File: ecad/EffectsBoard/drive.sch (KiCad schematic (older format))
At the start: 11 parts, among them U1 RC4558

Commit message: Rearrange schematics
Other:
- moved on the sheet: 51p1, C5, C6, D2, D3, R10, R7, R8, R9, RV1, U1A

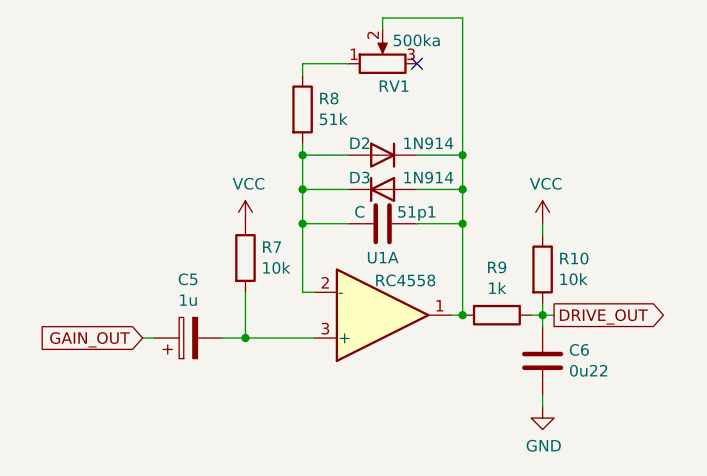
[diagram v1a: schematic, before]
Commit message: Fix annotation
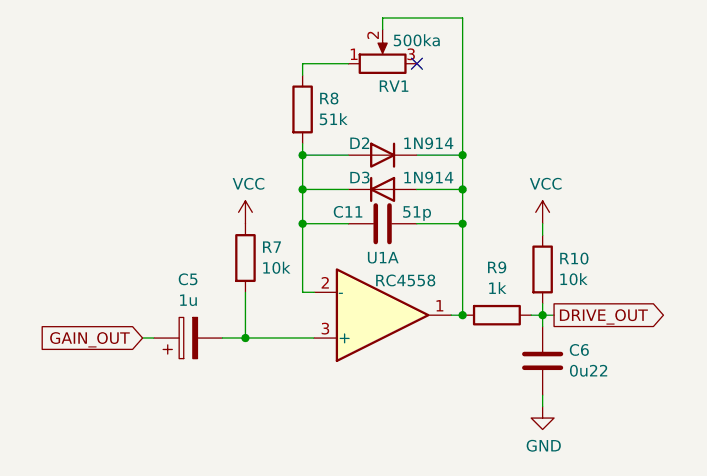
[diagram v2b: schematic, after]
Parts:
- C11: renamed from 51p1; value C -> 51p
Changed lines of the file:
@@
 P 1950 1400
 AR Path="/60325725" Ref="51p?"  Part="1"
-AR Path="/603069E8/60325725" Ref="51p1"  Part="1"
-F 0 "51p1" V 1900 1550 50  0000 C CNN
-F 1 "C" V 1900 1300 50  0000 C CNN
+AR Path="/603069E8/60325725" Ref="C11"  Part="1"
+F 0 "C11" V 1900 1250 50  0000 C CNN
+F 1 "51p" V 1900 1550 50  0000 C CNN
 F 2 "" H 1988 1250 50  0001 C CNN
 F 3 "~" H 1950 1400 50  0001 C CNN

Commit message: Update ecad autosave
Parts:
- C11, C5, C6: footprint (none) -> Capacitor_SMD:C_0805_2012Metric_Pad1.18x1.45mm_HandSolder
- R10, R7, R8, R9: footprint (none) -> Resistor_SMD:R_0805_2012Metric_Pad1.20x1.40mm_HandSolder
- RV1: footprint (none) -> screaming-panda:Potentiometer_Bourns_PTV09A-1_Single_Vertical
- U1: footprint (none) -> Package_SO:Texas_R-PDSO-G8_EP2.95x4.9mm_Mask2.4x3.1mm
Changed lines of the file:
@@
 F 0 "C5" V 1355 1900 50  0000 C CNN
 F 1 "1u" V 1264 1900 50  0000 C CNN
-F 2 "" H 1138 1750 50  0001 C CNN
+F 2 "Capacitor_SMD:C_0805_2012Metric_Pad1.18x1.45mm_HandSolder" H 1138 1750 50  0001 C CNN
 F 3 "~" H 1100 1900 50  0001 C CNN
 	1    1100 1900
@@
 F 0 "U1" H 1950 1550 50  0000 C CNN
 F 1 "RC4558" H 2050 1650 50  0000 C CNN
-F 2 "" H 1950 1800 50  0001 C CNN
+F 2 "Package_SO:Texas_R-PDSO-G8_EP2.95x4.9mm_Mask2.4x3.1mm" H 1950 1800 50  0001 C CNN
 F 3 "http://www.ti.com/lit/ds/symlink/rc4558.pdf" H 1950 1800 50  0001 C CNN
 	1    1950 1800
@@
 F 0 "C11" V 1900 1250 50  0000 C CNN
 F 1 "51p" V 1900 1550 50  0000 C CNN
-F 2 "" H 1988 1250 50  0001 C CNN
+F 2 "Capacitor_SMD:C_0805_2012Metric_Pad1.18x1.45mm_HandSolder" H 1988 1250 50  0001 C CNN
 F 3 "~" H 1950 1400 50  0001 C CNN
 	1    1950 1400
@@
 F 0 "R8" H 1670 946 50  0000 L CNN
 F 1 "51k" H 1670 855 50  0000 L CNN
-F 2 "" V 1530 900 50  0001 C CNN
+F 2 "Resistor_SMD:R_0805_2012Metric_Pad1.20x1.40mm_HandSolder" V 1530 900 50  0001 C CNN
 F 3 "~" H 1600 900 50  0001 C CNN
 	1    1600 900
@@
 F 0 "RV1" V 1850 650 50  0000 C CNN
 F 1 "500ka" V 2050 550 50  0000 C CNN
-F 2 "" H 1950 700 50  0001 C CNN
+F 2 "screaming-panda:Potentiometer_Bourns_PTV09A-1_Single_Vertical" H 1950 700 50  0001 C CNN
 F 3 "~" H 1950 700 50  0001 C CNN
 	1    1950 700
@@
 F 0 "R9" V 2243 1800 50  0000 C CNN
 F 1 "1k" V 2334 1800 50  0000 C CNN
-F 2 "" V 2380 1800 50  0001 C CNN
+F 2 "Resistor_SMD:R_0805_2012Metric_Pad1.20x1.40mm_HandSolder" V 2380 1800 50  0001 C CNN
 F 3 "~" H 2450 1800 50  0001 C CNN
 	1    2450 1800
@@
 F 0 "R10" H 2720 1646 50  0000 L CNN
 F 1 "10k" H 2720 1555 50  0000 L CNN
-F 2 "" V 2580 1600 50  0001 C CNN
+F 2 "Resistor_SMD:R_0805_2012Metric_Pad1.20x1.40mm_HandSolder" V 2580 1600 50  0001 C CNN
 F 3 "~" H 2650 1600 50  0001 C CNN
 	1    2650 1600
@@
 F 0 "C6" H 2765 2046 50  0000 L CNN
 F 1 "0u22" H 2765 1955 50  0000 L CNN
-F 2 "" H 2688 1850 50  0001 C CNN
+F 2 "Capacitor_SMD:C_0805_2012Metric_Pad1.18x1.45mm_HandSolder" H 2688 1850 50  0001 C CNN
 F 3 "~" H 2650 2000 50  0001 C CNN
 	1    2650 2000
@@
 F 0 "R7" H 1420 1596 50  0000 L CNN
 F 1 "10k" H 1420 1505 50  0000 L CNN
-F 2 "" V 1280 1550 50  0001 C CNN
+F 2 "Resistor_SMD:R_0805_2012Metric_Pad1.20x1.40mm_HandSolder" V 1280 1550 50  0001 C CNN
 F 3 "~" H 1350 1550 50  0001 C CNN
 	1    1350 1550
